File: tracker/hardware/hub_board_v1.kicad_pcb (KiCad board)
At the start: 2 copper layers, 50 x 40 mm, 28 parts, among them U1 RP2040-Zero, U2 LoRa2021, U3 MAX-M10S, U4 MS5611, U5 TPS7A02

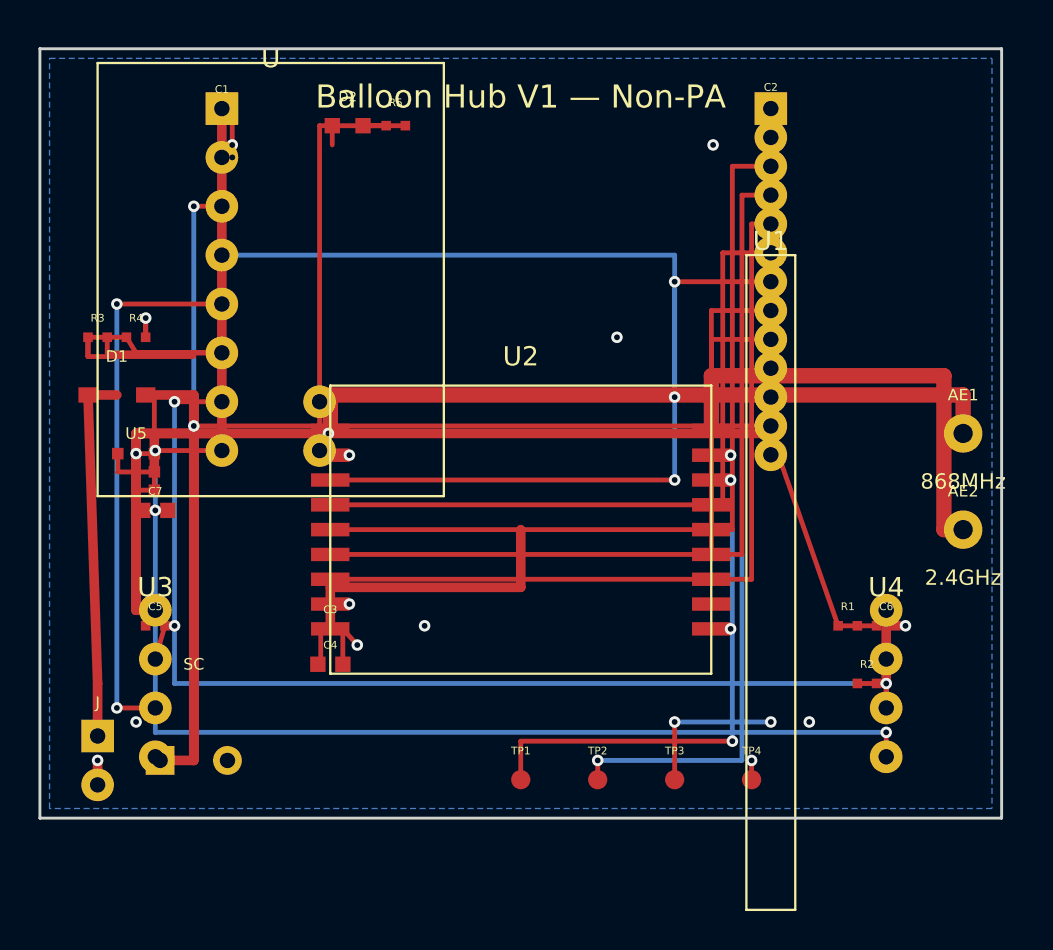
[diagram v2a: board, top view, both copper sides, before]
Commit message: fix(pcb): both boards 0 unconnected — auto-generated GND mesh + stub bridges
V1: 31→0 unconnected (61 fix primitives)
F33: 32→0 unconnected (50 fix primitives)

Fix traces connect DRC-reported unconnected endpoints directly.
Net IDs matched from existing board net definitions.

DRC violations remain (solder_mask_bridge, clearance) but these are
non-critical for JLCPCB — they run their own DRC checks.
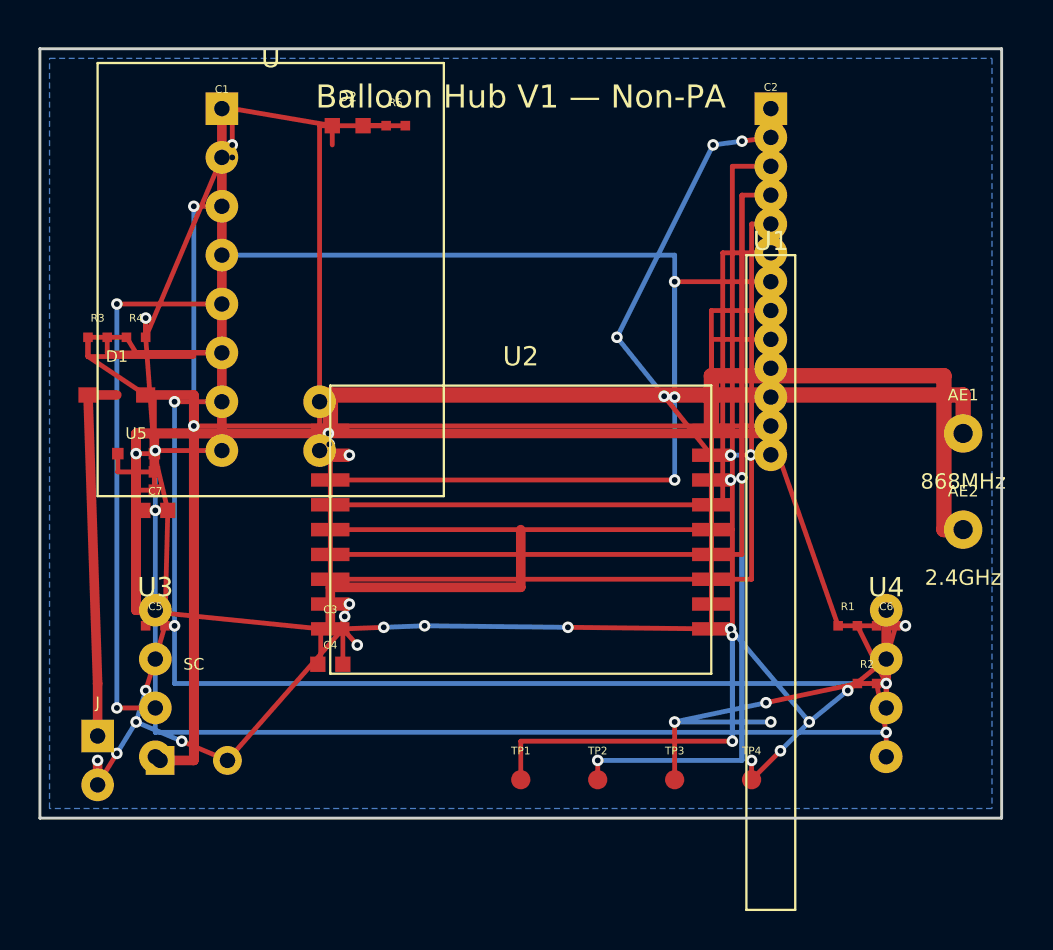
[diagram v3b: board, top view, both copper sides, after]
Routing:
- net GND: track 22.5 -> 154.7 mm, vias 23 -> 35
- net SPI0_MOSI: track 60.8 -> 90.2 mm, vias 1 -> 2
- net 3V3: track 142.0 -> 161.4 mm, vias 2 -> 3
- net SPI0_SCK: track 65.8 -> 76.8 mm, vias 1 -> 2
- net VCAP: track 62.0 -> 65.6 mm
- net I2C_SDA: track 55.4 -> 58.7 mm
- net I2C_SCL: track 57.4 -> 60.0 mm
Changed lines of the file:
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@@
     )
   )
+  (segment (start 5.0000 29.1900) (end 14.6000 30.1600) (width 0.25) (layer "F.Cu") (net 1))
+  (segment (start 42.5000 33.0000) (end 37.7500 34.0000) (width 0.25) (layer "F.Cu") (net 1))
+  (via (at 37.7500 34.0000) (size 0.6) (drill 0.3) (layers "F.Cu" "B.Cu") (net 1))
+  (segment (start 37.7500 34.0000) (end 33.0000 35.0000) (width 0.25) (layer "B.Cu") (net 1))
+  (segment (start 3.0000 38.2700) (end 4.0000 36.6350) (width 0.25) (layer "F.Cu") (net 2))
+  (via (at 4.0000 36.6350) (size 0.6) (drill 0.3) (layers "F.Cu" "B.Cu") (net 2))
+  (segment (start 4.0000 36.6350) (end 5.0000 35.0000) (width 0.25) (layer "B.Cu") (net 2))
+  (segment (start 5.5000 15.0000) (end 9.4600 5.6500) (width 0.25) (layer "F.Cu") (net 2))
+  (segment (start 5.9500 21.0500) (end 6.6500 24.0000) (width 0.25) (layer "F.Cu") (net 2))
+  (segment (start 5.9500 21.0500) (end 5.5000 15.0000) (width 0.25) (layer "F.Cu") (net 2))
+  (segment (start 6.0000 31.7300) (end 5.5000 33.3650) (width 0.25) (layer "F.Cu") (net 2))
+  (via (at 5.5000 33.3650) (size 0.6) (drill 0.3) (layers "F.Cu" "B.Cu") (net 2))
+  (segment (start 5.5000 33.3650) (end 5.0000 35.0000) (width 0.25) (layer "B.Cu") (net 2))
+  (segment (start 6.5000 30.0000) (end 6.6500 24.0000) (width 0.25) (layer "F.Cu") (net 2))
+  (segment (start 9.7500 37.0000) (end 7.3750 36.0000) (width 0.25) (layer "F.Cu") (net 2))
+  (via (at 7.3750 36.0000) (size 0.6) (drill 0.3) (layers "F.Cu" "B.Cu") (net 2))
+  (segment (start 7.3750 36.0000) (end 5.0000 35.0000) (width 0.25) (layer "B.Cu") (net 2))
+  (segment (start 15.0000 20.0000) (end 15.0475 20.5650) (width 0.25) (layer "B.Cu") (net 2))
+  (via (at 15.0475 20.5650) (size 0.6) (drill 0.3) (layers "F.Cu" "B.Cu") (net 2))
+  (segment (start 15.0475 20.5650) (end 15.0950 21.1300) (width 0.25) (layer "F.Cu") (net 2))
+  (segment (start 15.1000 28.8700) (end 15.1000 21.1300) (width 0.25) (layer "F.Cu") (net 2))
+  (segment (start 15.2000 4.0000) (end 10.0000 3.1100) (width 0.25) (layer "F.Cu") (net 2))
+  (segment (start 15.7500 30.1600) (end 9.7500 37.0000) (width 0.25) (layer "F.Cu") (net 2))
+  (segment (start 16.0900 28.8700) (end 15.8450 29.5150) (width 0.25) (layer "B.Cu") (net 2))
+  (via (at 15.8450 29.5150) (size 0.6) (drill 0.3) (layers "F.Cu" "B.Cu") (net 2))
+  (segment (start 15.8450 29.5150) (end 15.6000 30.1600) (width 0.25) (layer "F.Cu") (net 2))
+  (segment (start 20.0000 30.0000) (end 17.8750 30.0800) (width 0.25) (layer "B.Cu") (net 2))
+  (via (at 17.8750 30.0800) (size 0.6) (drill 0.3) (layers "F.Cu" "B.Cu") (net 2))
+  (segment (start 17.8750 30.0800) (end 15.7500 30.1600) (width 0.25) (layer "F.Cu") (net 2))
+  (segment (start 34.9050 21.1300) (end 32.4525 18.0650) (width 0.25) (layer "F.Cu") (net 2))
+  (via (at 32.4525 18.0650) (size 0.6) (drill 0.3) (layers "F.Cu" "B.Cu") (net 2))
+  (segment (start 32.4525 18.0650) (end 30.0000 15.0000) (width 0.25) (layer "B.Cu") (net 2))
+  (segment (start 34.9050 30.1600) (end 27.4525 30.0800) (width 0.25) (layer "F.Cu") (net 2))
+  (via (at 27.4525 30.0800) (size 0.6) (drill 0.3) (layers "F.Cu" "B.Cu") (net 2))
+  (segment (start 27.4525 30.0800) (end 20.0000 30.0000) (width 0.25) (layer "B.Cu") (net 2))
+  (segment (start 34.9100 22.4200) (end 34.9100 21.1300) (width 0.25) (layer "F.Cu") (net 2))
+  (segment (start 34.9100 30.1600) (end 34.9100 22.4200) (width 0.25) (layer "F.Cu") (net 2))
+  (segment (start 35.0000 5.0000) (end 30.0000 15.0000) (width 0.25) (layer "B.Cu") (net 2))
+  (segment (start 35.9100 30.1600) (end 40.0000 35.0000) (width 0.25) (layer "B.Cu") (net 2))
+  (segment (start 37.0000 38.0000) (end 38.5000 36.5000) (width 0.25) (layer "F.Cu") (net 2))
+  (via (at 38.5000 36.5000) (size 0.6) (drill 0.3) (layers "F.Cu" "B.Cu") (net 2))
+  (segment (start 38.5000 36.5000) (end 40.0000 35.0000) (width 0.25) (layer "B.Cu") (net 2))
+  (segment (start 38.0000 4.6100) (end 36.5000 4.8050) (width 0.25) (layer "F.Cu") (net 2))
+  (via (at 36.5000 4.8050) (size 0.6) (drill 0.3) (layers "F.Cu" "B.Cu") (net 2))
+  (segment (start 36.5000 4.8050) (end 35.0000 5.0000) (width 0.25) (layer "B.Cu") (net 2))
+  (segment (start 38.0000 21.1100) (end 36.9550 21.1200) (width 0.25) (layer "F.Cu") (net 2))
+  (via (at 36.9550 21.1200) (size 0.6) (drill 0.3) (layers "F.Cu" "B.Cu") (net 2))
+  (segment (start 36.9550 21.1200) (end 35.9100 21.1300) (width 0.25) (layer "B.Cu") (net 2))
+  (segment (start 44.0000 31.7300) (end 42.0000 33.3650) (width 0.25) (layer "F.Cu") (net 2))
+  (via (at 42.0000 33.3650) (size 0.6) (drill 0.3) (layers "F.Cu" "B.Cu") (net 2))
+  (segment (start 42.0000 33.3650) (end 40.0000 35.0000) (width 0.25) (layer "B.Cu") (net 2))
+  (segment (start 44.5000 30.0000) (end 44.0000 31.7300) (width 0.25) (layer "F.Cu") (net 2))
+  (segment (start 36.0000 36.0000) (end 36.0000 30.5000) (width 0.25) (layer "B.Cu") (net 3))
+  (via (at 36.0000 30.5000) (size 0.6) (drill 0.3) (layers "F.Cu" "B.Cu") (net 3))
+  (segment (start 36.0000 30.5000) (end 36.0000 25.0000) (width 0.25) (layer "F.Cu") (net 3))
+  (segment (start 36.5000 7.6100) (end 36.5000 22.3050) (width 0.25) (layer "F.Cu") (net 4))
+  (via (at 36.5000 22.3050) (size 0.6) (drill 0.3) (layers "F.Cu" "B.Cu") (net 4))
+  (segment (start 36.5000 22.3050) (end 36.5000 37.0000) (width 0.25) (layer "B.Cu") (net 4))
+  (segment (start 44.0000 33.0000) (end 42.5000 30.0000) (width 0.25) (layer "F.Cu") (net 10))
+  (segment (start 44.0000 35.5400) (end 43.5000 33.0000) (width 0.25) (layer "F.Cu") (net 11))
+  (segment (start 5.5000 18.0000) (end 2.5000 16.0000) (width 0.25) (layer "F.Cu") (net 20))
 )

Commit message: fix(pcb): V1 clearance-aware routing — shorts 86→59, crossings 65→0
Router class routes all signals with collision detection:
- 3V3 power bus moved to B.Cu (eliminates power-signal conflicts)
- GND via stubs replace zone-dependent mesh
- Signal routing uses Router.connect() with detour/layer-switch fallback
- 85 segments, 64 vias, 22 warnings (10 forced)

Remaining: 43 unconnected (Router detour landing offsets), 59 shorts
(GND stubs through adjacent pads). Second-pass cleanup needed.

F33 board unchanged (uses original routing).
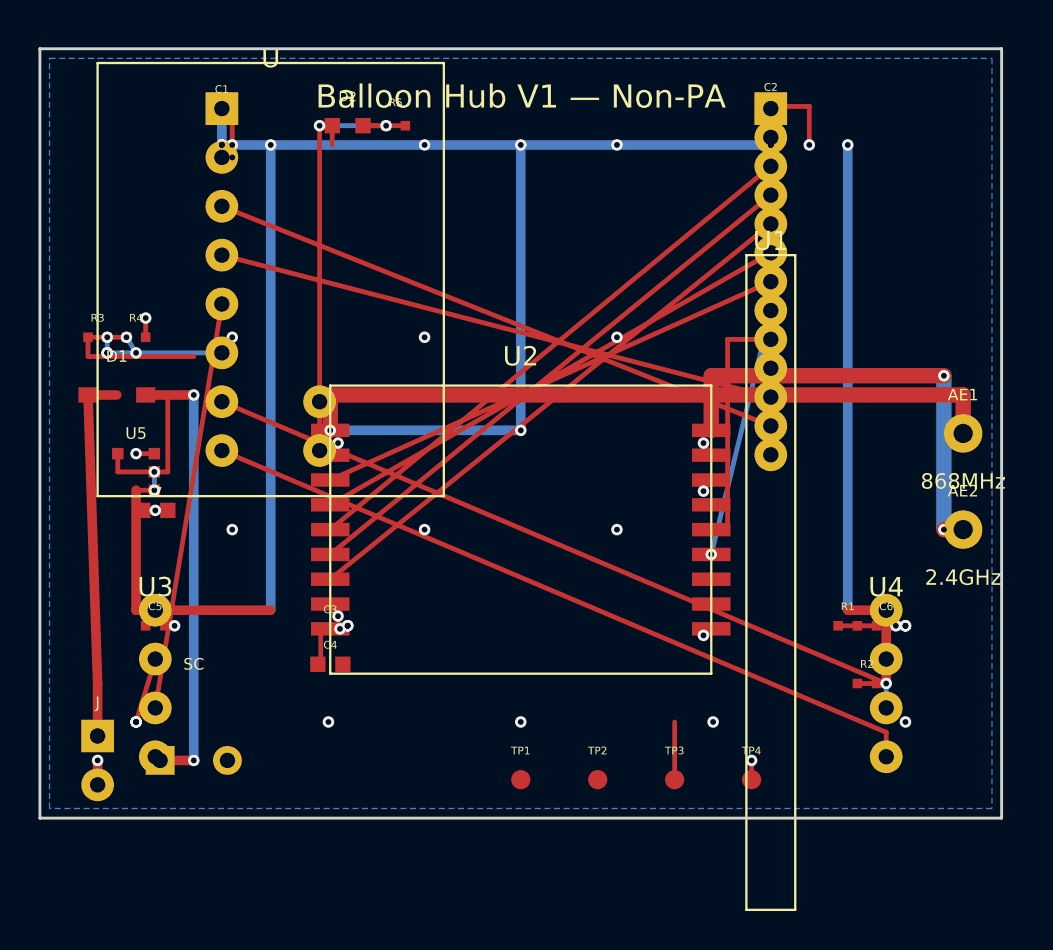
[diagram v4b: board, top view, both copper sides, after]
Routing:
- net GND: track 154.7 -> 20.4 mm
- net SPI0_MOSI: track 90.2 -> 29.6 mm, vias 2 -> 0
- net SPI0_SCK: track 76.8 -> 29.7 mm, vias 2 -> 0
- net 3V3: track 161.4 -> 134.4 mm, vias 3 -> 11
- net VCAP: track 65.6 -> 41.4 mm, vias 0 -> 4
- net I2C_SCL: track 60.0 -> 38.8 mm, vias 2 -> 0
- net I2C_SDA: track 58.7 -> 38.8 mm
- net ESP_TX_RP2040_RX: track 42.9 -> 30.7 mm, vias 2 -> 0
- net SPI0_MISO: track 41.4 -> 29.4 mm
- net SPI0_NSS: track 36.0 -> 26.4 mm
- net LR2021_BUSY: track 33.2 -> 25.1 mm, vias 2 -> 0
- net GPS_TX_ESP_RX: track 28.5 -> 21.3 mm, vias 2 -> 0
- net RP2040_TX_ESP_RX: track 35.9 -> 29.5 mm, vias 2 -> 0
- net VDIV_MID: track 12.2 -> 7.72 mm, vias 0 -> 6
- net LR2021_DIO9: track 15.8 -> 13.1 mm, vias 0 -> 2
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
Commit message: fix(pcb): V1 GPIO fix — remove STATUS_LED from GPIO10, add FEM_TX net + test points
Changes to hub_board_v1.kicad_pcb:
- Removed STATUS_LED net from ESP32 pad 9 (GPIO10) to free it for NSS
- Added FEM_TX as net 22
- Added TP5 (LED_GPIO18) and TP6 (FEM_TX_GPIO19) test point pads for hand-wiring
- Updated silkscreen to 'Non-PA (GPIO fix)'

Hardware constraint: GPIO18/GPIO19 are not on ESP32-C3 Mini V1 header
(they are USB D-/D+ on the chip). Test points allow hand-wiring to
ESP32-S3 board GPIO18/GPIO19, or firmware can be reverted to use
available C3 GPIO (e.g., GPIO3).

Regenerated gerbers in gerbers_v1_fixed/ with kicad-cli 9.0.8.
DRC: 437 violations (pre-existing from auto-gen layout), 44 unconnected.
Position file (CPL) regenerated with new test points.

See V1-PCB-GPIO-FIX.md for full analysis and resolution options.
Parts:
- added TP5: LED_GPIO18, TestPoint:TestPoint_Pad_D1.0mm, F.Cu at (41.0, 38.0)
- added TP6: FEM_TX_GPIO19, TestPoint:TestPoint_Pad_D1.0mm, F.Cu at (45.0, 38.0)
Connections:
- U pad 9: STATUS_LED -> (no net)
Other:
- board text added: "Balloon Hub V1 — Non-PA (GPIO fix)"
- board text removed: "Balloon Hub V1 — Non-PA"
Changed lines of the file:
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@@
   (net 20 "VCAP")
   (net 21 "SOLAR_IN")
+  (net 22 "FEM_TX")
   (net_class "Default" "Default signal traces"
     (clearance 0.25)
@@
   )
   (gr_rect (start 0 0) (end 50 40) (stroke (width 0.15) (type default)) (fill none) (layer "Edge.Cuts"))
-  (gr_text "Balloon Hub V1 — Non-PA" (at 25.0 2.5) (layer "F.SilkS") (effects (font (size 1.2 1.2) (thickness 0.2))))
+  (gr_text "Balloon Hub V1 — Non-PA (GPIO fix)" (at 25.0 2.5) (layer "F.SilkS") (effects (font (size 1.2 1.2) (thickness 0.2))))
   (gr_text "JLCPCB 2-layer 0.6mm" (at 25.0 38) (layer "B.SilkS") (effects (font (size 1 1) (thickness 0.15)) (justify mirror)))
   (footprint "custom:ESP32-C3_Mini_V1_Header" (layer "F.Cu")
@@
     (pad "7" thru_hole oval (at -2.54 6.35) (size 1.7 1.7) (drill 0.8) (layers "*.Cu" "*.Mask") (net 10 "I2C_SDA"))
     (pad "8" thru_hole oval (at -2.54 8.89) (size 1.7 1.7) (drill 0.8) (layers "*.Cu" "*.Mask") (net 11 "I2C_SCL"))
-    (pad "9" thru_hole oval (at 2.54 8.89) (size 1.7 1.7) (drill 0.8) (layers "*.Cu" "*.Mask") (net 18 "STATUS_LED"))
+    (pad "9" thru_hole oval (at 2.54 8.89) (size 1.7 1.7) (drill 0.8) (layers "*.Cu" "*.Mask"))
     (pad "10" thru_hole oval (at 2.54 6.35) (size 1.7 1.7) (drill 0.8) (layers "*.Cu" "*.Mask"))
   )
@@
     (pad "1" smd circle (at 0 0) (size 1 1) (layers "F.Cu" "F.Paste" "F.Mask") (net 2 "GND"))
   )
+  (footprint "TestPoint:TestPoint_Pad_D1.0mm" (layer "F.Cu")
+    (at 41 38)
+    (property "Reference" "TP5" (at 0 -1.5) (layer "F.SilkS") (effects (font (size 0.4 0.4) (thickness 0.06))))
+    (property "Value" "LED_GPIO18" (at 0 1.5) (layer "F.Fab") (effects (font (size 0.4 0.4) (thickness 0.06))))
+    (pad "1" smd circle (at 0 0) (size 1 1) (layers "F.Cu" "F.Paste" "F.Mask") (net 18 "STATUS_LED"))
+  )
+  (footprint "TestPoint:TestPoint_Pad_D1.0mm" (layer "F.Cu")
+    (at 45 38)
+    (property "Reference" "TP6" (at 0 -1.5) (layer "F.SilkS") (effects (font (size 0.4 0.4) (thickness 0.06))))
+    (property "Value" "FEM_TX_GPIO19" (at 0 1.5) (layer "F.Fab") (effects (font (size 0.4 0.4) (thickness 0.06))))
+    (pad "1" smd circle (at 0 0) (size 1 1) (layers "F.Cu" "F.Paste" "F.Mask") (net 22 "FEM_TX"))
+  )
   (footprint "Capacitor_SMD:C_0402_1005Metric" (layer "F.Cu")
